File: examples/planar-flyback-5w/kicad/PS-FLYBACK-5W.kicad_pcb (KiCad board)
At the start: 6 copper layers, 44 x 94 mm, 29 parts, among them J1 18-36 V DC, J2 5 V / 1 A isolated, T1 PLANAR 4:2 / Lm 13.12uH, U1 LT8302IS8E#PBF

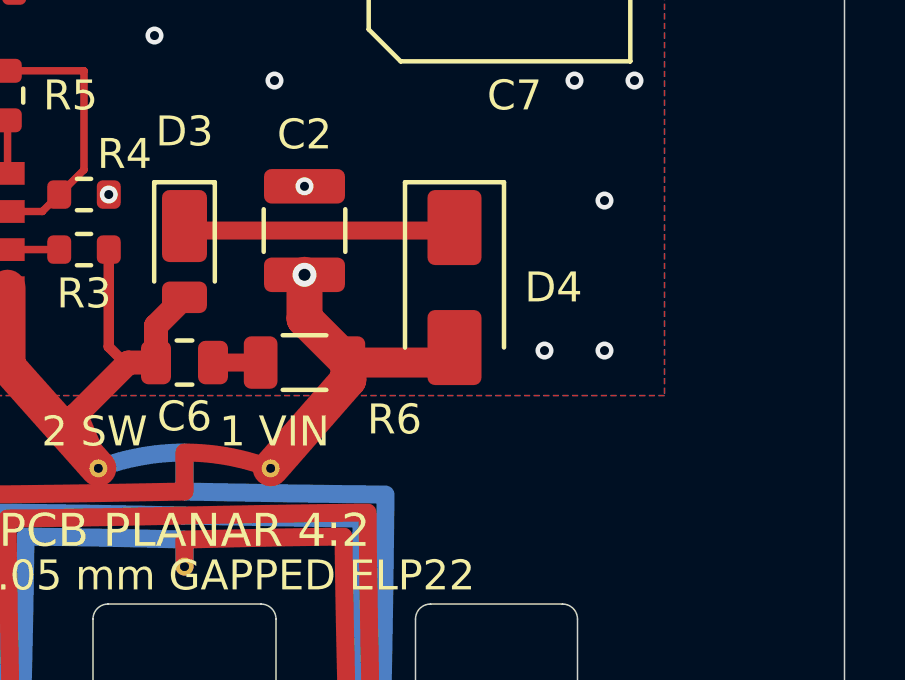
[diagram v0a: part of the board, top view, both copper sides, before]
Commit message: Upgrade flyback snubber to 2 W 2512 and regenerate A5 handoff
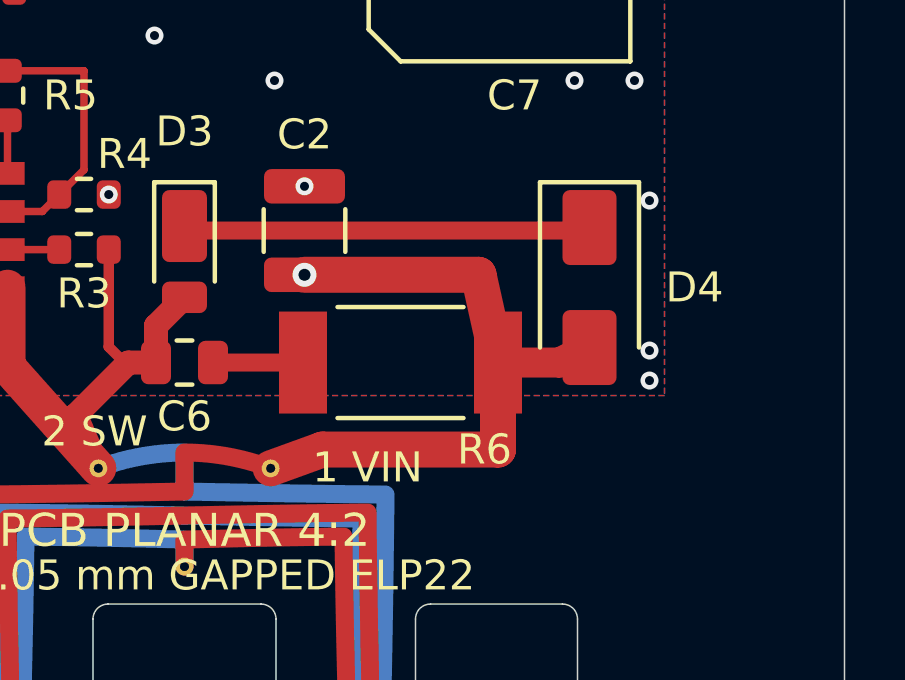
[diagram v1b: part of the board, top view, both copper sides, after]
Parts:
- R6: value 39R 0.75 W -> 39R 2 W; footprint Flyback:R_1206_3216Metric -> Flyback:R_EverOhms_CRH2512
- moved D4 4.50 mm to (113.5, 65.9)
- moved R6 3.20 mm to (107.2, 68.4)
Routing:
- net /VIN: track 61.1 -> 71.9 mm
- net /CLAMP: track 9.10 -> 13.6 mm
- net /SNUB: track 1.59 -> 3.00 mm
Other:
- board text added: "A5 ENGINEERING PROTOTYPE"
- board text removed: "A4 ENGINEERING PROTOTYPE"

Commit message: fix(flyback): center secondary routing and strengthen preload margin
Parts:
- R7: value 220R 0.25 W -> 180R 0.25 W
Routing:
- net /SEC_A: track 9.29 -> 10.2 mm
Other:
- board text added: "A6 ENGINEERING PROTOTYPE"
- board text removed: "A5 ENGINEERING PROTOTYPE"

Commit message: fix(flyback): select OSP and replace short-stock UVLO resistor
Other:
- board text added: "A7 ENGINEERING PROTOTYPE"
- board text removed: "A6 ENGINEERING PROTOTYPE"

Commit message: Fix flyback SW winding short and publish verified A8 files
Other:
- board text added: "A8 ENGINEERING PROTOTYPE"
- board text removed: "A7 ENGINEERING PROTOTYPE"

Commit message: Fix flyback turn spacing and document PCB integration pitfalls
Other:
- board text added: "A9 ENGINEERING PROTOTYPE"
- board text added: "Net-tie DRC cannot prove winding topology or turn spacing."
- board text added: "Run winding checks; see COMMON-ISSUES.md for known failure modes."
- board text added: "T1: 0.25 mm nominal turn spacing / 0.20 mm minimum copper gap"
- board text removed: "A8 ENGINEERING PROTOTYPE"

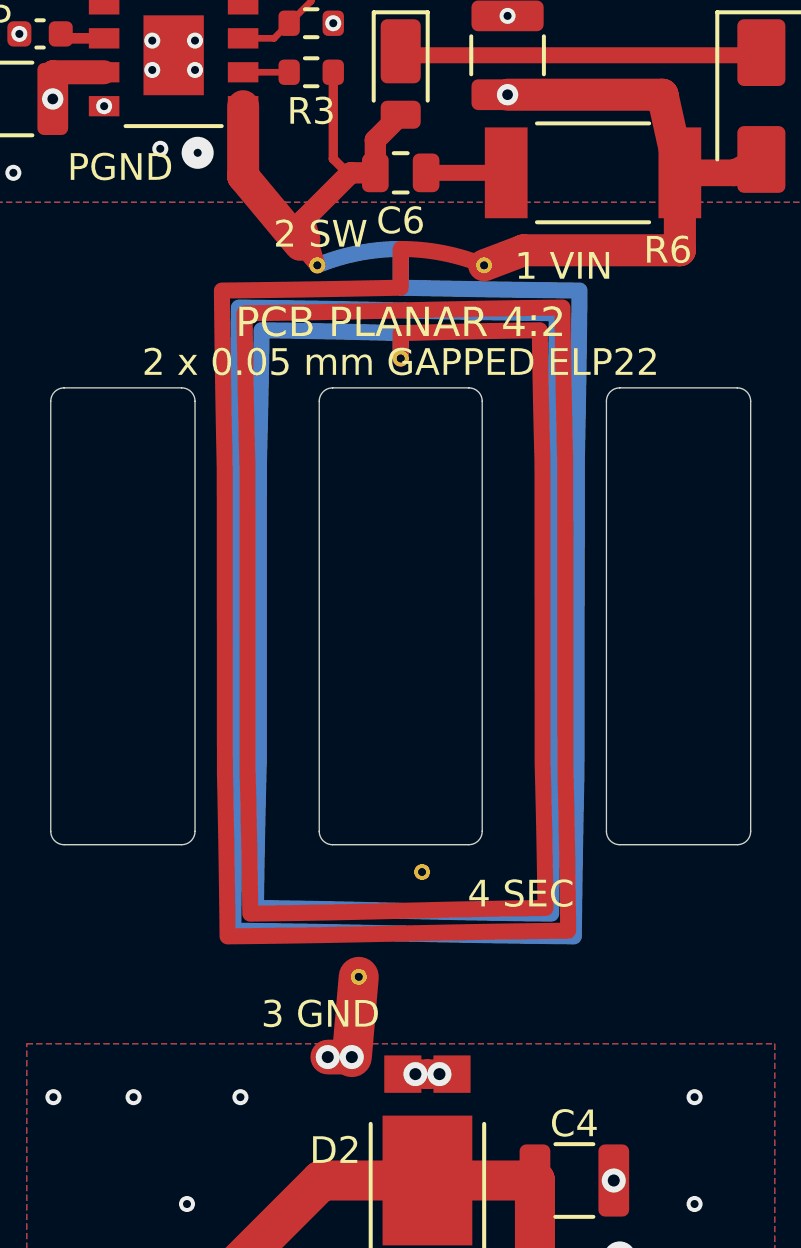
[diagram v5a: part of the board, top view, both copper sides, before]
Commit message: Fix flyback winding and via clearances in A10
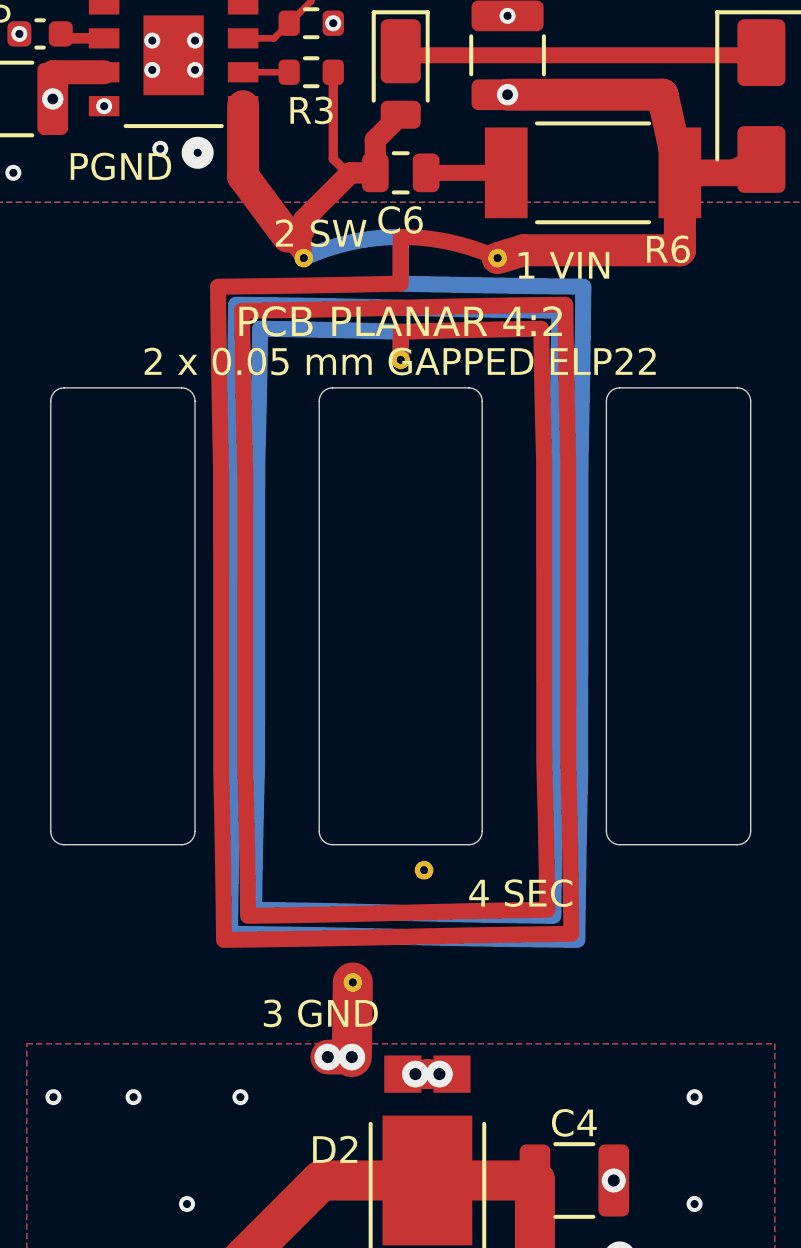
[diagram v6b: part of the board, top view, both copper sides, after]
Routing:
- net /SW: track 18.8 -> 18.0 mm
- net /VIN: track 71.7 -> 71.1 mm
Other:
- board text added: "A10 ENGINEERING PROTOTYPE"
- board text added: "T1 lands 0.70/0.30 mm; paired secondary via lands 1.00/0.45 mm."
- board text added: "T1: 0.30 mm nominal spacing / >=0.26 mm verified CAD turn gap"
- board text removed: "A9 ENGINEERING PROTOTYPE"
- board text removed: "T1: 0.25 mm nominal turn spacing / 0.20 mm minimum copper gap"
